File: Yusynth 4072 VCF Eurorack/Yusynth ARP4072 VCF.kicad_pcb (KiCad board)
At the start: 2 copper layers, 39.4 x 99.7 mm, 85 parts, among them J1 Audio In 1, J2 Audio In 2, J3 V/Oct, J4 CV 1, J5 CV 2, J6 Audio In 1, J7 CONN_02X05, Q1 MMDT3906, Q2 MMDT3906, Q3 MMDT3906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

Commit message: Minor corrections
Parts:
- added REF**: VIA-0.6mm, YusynthLib:VIA-0.6mm, F.Cu at (175.4, 68.1)
- J6: value Audio In 1 -> Audio Out
- moved R14 16.5 mm to (163.8, 118.1), turned to 180 degrees
- moved J1 16.5 mm to (186.7, 154.9)
- moved J2 16.5 mm to (174.0, 154.9)
- moved J4 16.5 mm to (186.7, 138.4)
- moved J5 16.5 mm to (174.0, 138.4)
- moved REF** 8.98 mm to (172.7, 118.1)
- moved Q2 6.29 mm to (165.1, 133.3)
- moved R42 5.39 mm to (177.8, 134.0), turned to 90 degrees
- moved R2 3.81 mm to (163.8, 123.2)
- moved R43 0.20 mm to (174.0, 141.2)
- turned R39 to 90 degrees
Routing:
- net Net-(J1-Pad1): track 5.29 -> 59.5 mm
- net Earth: track 42.8 -> 67.8 mm
- net Net-(J5-Pad1): track 62.6 -> 41.9 mm, vias 1 -> 0
- net Net-(J2-Pad1): track 14.7 -> 33.8 mm, vias 1 -> 2
- net Net-(Q1-Pad5): track 23.1 -> 5.87 mm
- net Net-(J4-Pad1): track 55.2 -> 39.7 mm, vias 0 -> 1
- net -12V: track 194.3 -> 183.6 mm, vias 5 -> 3
- net Net-(C4-Pad2): track 99.5 -> 92.1 mm
- net Net-(Q1-Pad3): track 26.8 -> 32.8 mm
- net Net-(Q2-Pad1): track 6.30 -> 12.0 mm
- net Net-(C1-Pad2): track 43.9 -> 48.2 mm
- net Net-(Q2-Pad6): track 2.74 -> 6.23 mm
- net Net-(Q6-Pad2): track 15.4 -> 12.0 mm
- net Net-(C9-Pad1): track 63.0 -> 65.3 mm
- net Net-(R12-Pad2): track 85.0 -> 87.0 mm, vias 7 -> 6
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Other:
- outline, holes or cut-outs redrawn
- board text added: "Designed by Yves Usson"
- board text added: "PCB by Matt Reed"
- board text added: "Yusynth ARP VCF"
- board text removed: "Yusynth ARP VCF Designed by Yves Usson PCB by Matt Reed"

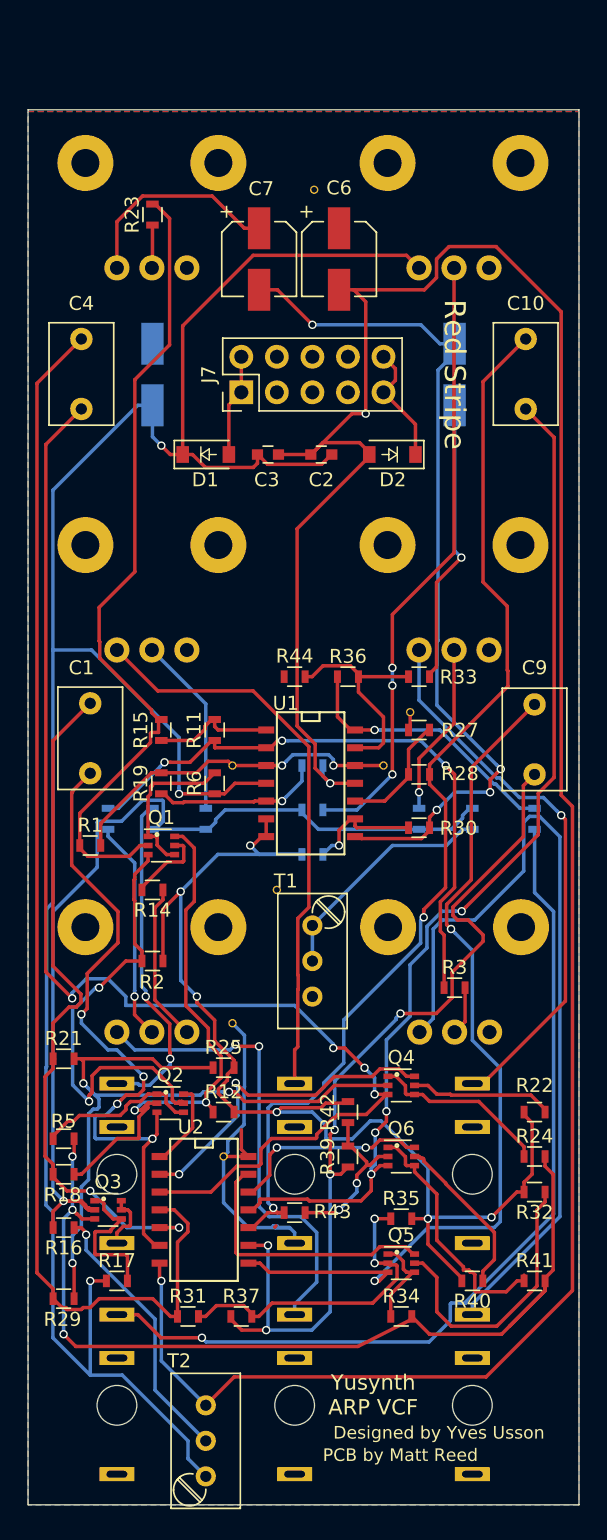
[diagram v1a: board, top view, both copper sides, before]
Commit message: updated board to use corrected thonkiconn lib. Wiring incomplete.
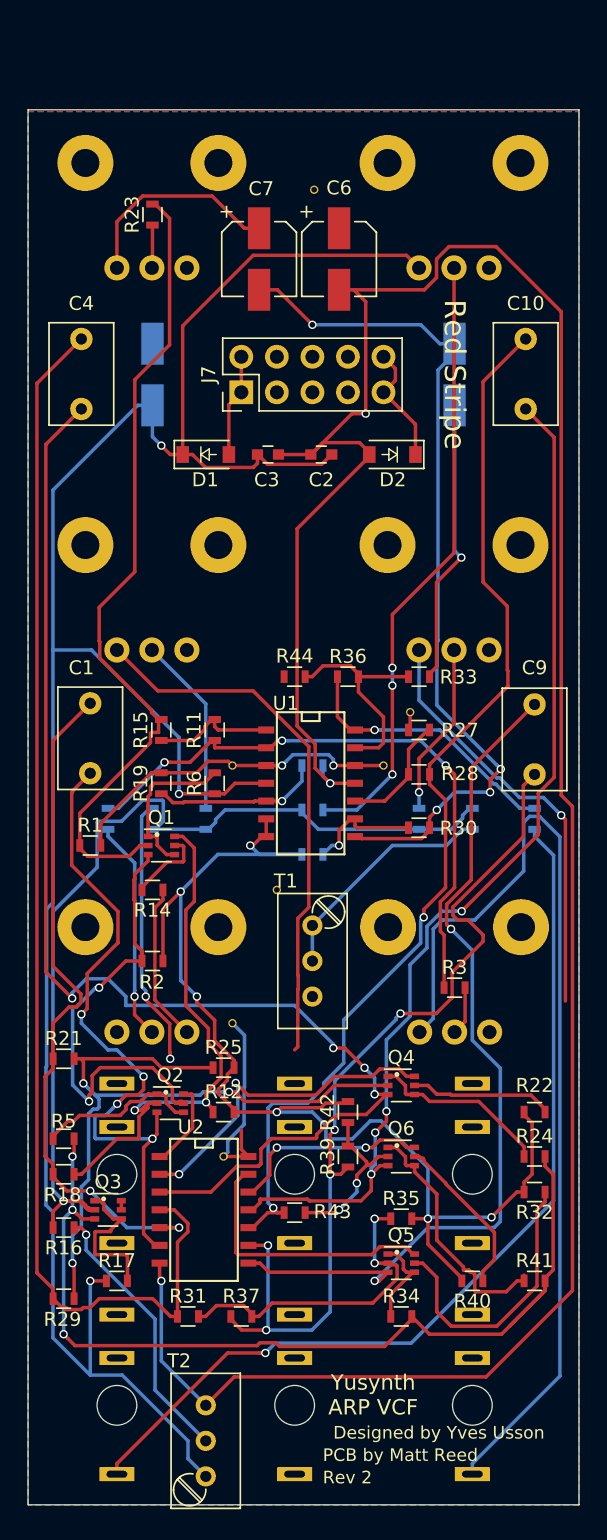
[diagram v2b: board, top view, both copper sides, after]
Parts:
- J1: footprint Thonkiconn:THONKICONN -> THONKICONN_Fixed
- J2, J3, J4, J5, J6: footprint Thonkiconn:THONKICONN -> YusynthLib:THONKICONN_Fixed
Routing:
- net Net-(J2-Pad1): track 33.8 -> 0.00 mm, vias 2 -> 0
- net Earth: track 67.8 -> 54.2 mm
- net Net-(J1-Pad1): track 59.5 -> 70.9 mm
- net Net-(J4-Pad1): track 39.7 -> 30.6 mm
- net Net-(J3-Pad1): track 24.1 -> 19.2 mm
- net Net-(J5-Pad1): track 41.9 -> 38.7 mm
- net Net-(J6-Pad1): track 64.6 -> 66.8 mm
- net Net-(Q3-Pad3): track 67.7 -> 68.2 mm
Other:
- board text added: "Rev 2"
